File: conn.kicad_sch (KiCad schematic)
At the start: 15 parts, among them J10 VIO2, J11 USB_C_Receptacle, J12 DIO, J13 GND, J14 AIN, J15 IO_IDC, J3 GND, J4 Field24V, J5 RJ45_LED_Shielded_x2, J6 PwrOut, J7 CAN, J8 CAN, J9 OUT

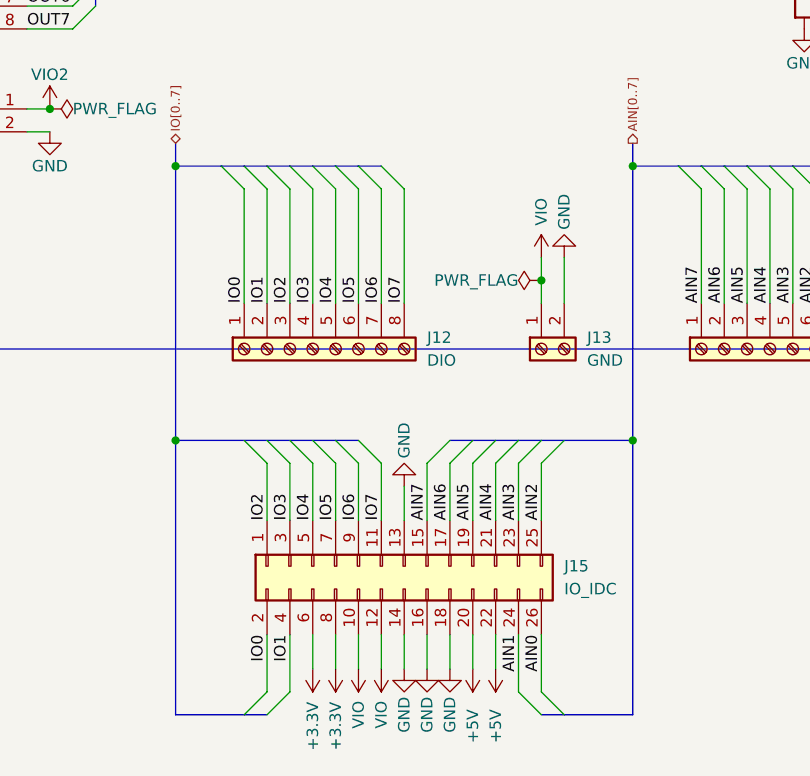
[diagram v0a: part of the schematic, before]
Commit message: Minimal design for testing
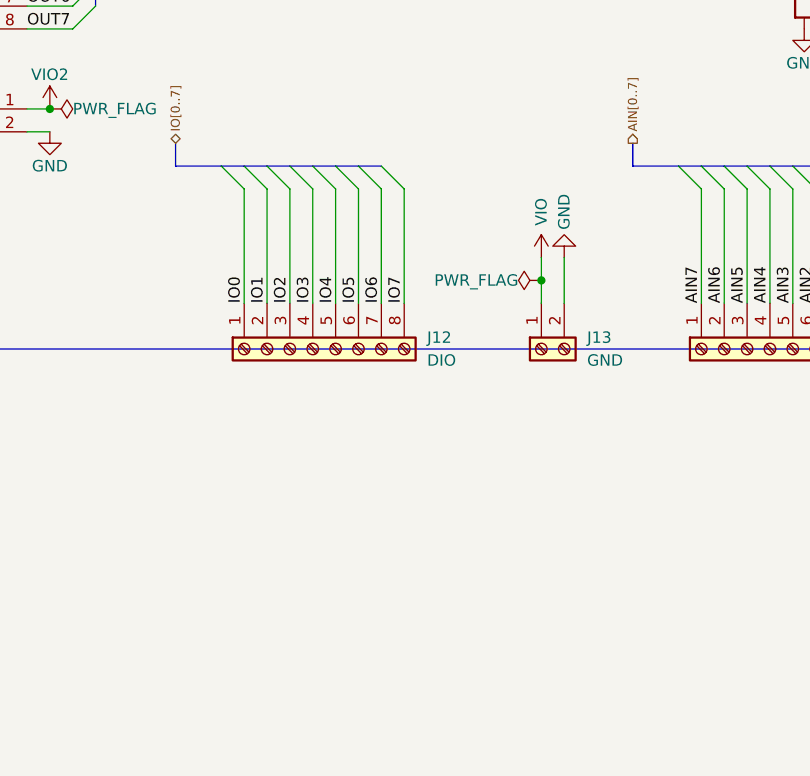
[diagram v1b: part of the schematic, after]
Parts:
- removed J15: IO_IDC, 71922:71922-126, symbol Connector_Generic:Conn_02x13_Odd_Even
